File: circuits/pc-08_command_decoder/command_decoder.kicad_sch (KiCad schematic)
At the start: 17 parts, among them U1 74HC138, U2 74HC138, U3 74HC138, U4 74HC138, U5 4011, U6 4011, U7 74HC138, U8 4011

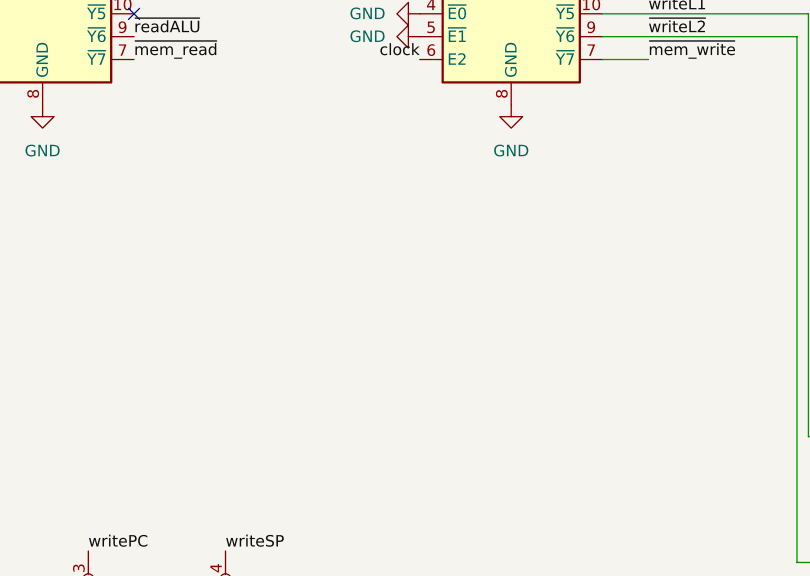
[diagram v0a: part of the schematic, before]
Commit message: add pull-up resistor network to command decoder
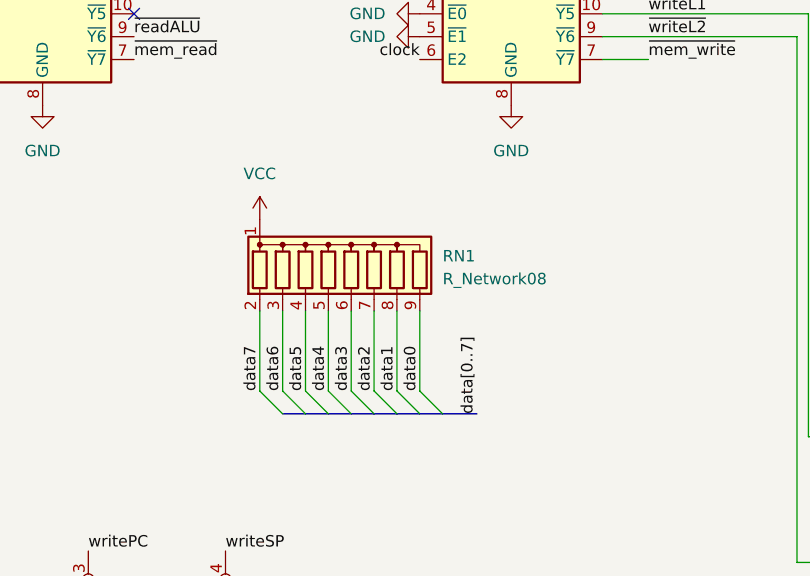
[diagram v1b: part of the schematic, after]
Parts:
- added RN1: R_Network08, Resistor_THT:R_Array_SIP9, symbol Device:R_Network08
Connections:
- net VCC: now also RN1.1 (common)
- net data0: now also RN1.9 (R8)
- net data1: now also RN1.8 (R7)
- net data2: now also RN1.7 (R6)
- net data3: now also RN1.6 (R5)
- net data4: now also RN1.5 (R4)
- net data5: now also RN1.4 (R3)
- net data6: now also RN1.3 (R2)
- net data7: now also RN1.2 (R1)

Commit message: pc08: finishing touches and interconnects
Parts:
- added D1: LED, LED_SMD:LED_0603_1608Metric, symbol Device:LED
- added J1: Screw_Terminal_01x02, TerminalBlock_TE-Connectivity:TerminalBlock_TE_282834-2_1x02_P2.54mm_Horizontal, symbol Connector:Screw_Terminal_01x02
- added J2: Conn_01x06, Connector_PinHeader_2.54mm:PinHeader_1x06_P2.54mm_Vertical, symbol Connector_Generic:Conn_01x06
- added J3: Conn_01x03, Connector_PinHeader_2.54mm:PinHeader_1x03_P2.54mm_Vertical, symbol Connector_Generic:Conn_01x03
- added J4: Conn_01x08, Connector_PinHeader_2.54mm:PinHeader_1x08_P2.54mm_Vertical, symbol Connector_Generic:Conn_01x08
- added J5: Conn_01x05, Connector_PinHeader_2.54mm:PinHeader_1x05_P2.54mm_Vertical, symbol Connector_Generic:Conn_01x05
- added J6: Conn_01x07, Connector_PinHeader_2.54mm:PinHeader_1x07_P2.54mm_Vertical, symbol Connector_Generic:Conn_01x07
- added R1: 1K, Resistor_SMD:R_0603_1608Metric, symbol Device:R
- added RN2, RN3: R_Network08, Resistor_THT:R_Array_SIP9, symbol Device:R_Network08
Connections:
- net GND: now also J1.1 (Pin_1), J6.7 (Pin_7), R1.2, RN2.1 (common), RN3.1 (common)
- net VCC: now also D1.2 (A), J1.2 (Pin_2), J6.1 (Pin_1)
- net action0: now also RN2.9 (R8)
- net action1: now also RN2.8 (R7)
- net action2: now also RN2.7 (R6)
- net action3: now also RN2.6 (R5)
- net action4: now also RN2.5 (R4)
- net asrc0: now also RN2.4 (R3)
- net asrc1: now also RN2.3 (R2)
- net asrc2: now also RN2.2 (R1)
- net carryFlag: now also J5.1 (Pin_1)
- net clock: now also J6.5 (Pin_5), RN3.2 (R1)
- net data0: now also J4.1 (Pin_1)
- net data1: now also J4.2 (Pin_2)
- net data2: now also J4.3 (Pin_3)
- net data3: now also J4.4 (Pin_4)
- net data4: now also J4.5 (Pin_5)
- net data5: now also J4.6 (Pin_6)
- net data6: now also J4.7 (Pin_7)
- net data7: now also J4.8 (Pin_8)
- net dsrc0: now also J5.2 (Pin_2), RN3.9 (R8)
- net dsrc1: now also J5.3 (Pin_3), RN3.8 (R7)
- net dsrc2: now also J5.4 (Pin_4), RN3.7 (R6)
- net dsrc3: now also J5.5 (Pin_5), RN3.6 (R5)
- net dtgt0: now also J6.2 (Pin_2), RN3.5 (R4)
- net dtgt1: now also J6.3 (Pin_3), RN3.4 (R3)
- net dtgt2: now also J6.4 (Pin_4), RN3.3 (R2)
- net ~{reset}: now also J6.6 (Pin_6)
- net at U1.7 (~{Y7}): now also J3.1 (Pin_1)
- net at U7.10 (~{Y5}): now also J2.4 (Pin_4)
- net at U7.11 (~{Y4}): now also J2.3 (Pin_3)
- net at U7.12 (~{Y3}): now also J2.2 (Pin_2)
- net at U7.13 (~{Y2}): now also J2.1 (Pin_1)
- net at U7.7 (~{Y7}): now also J2.6 (Pin_6)
- net at U7.9 (~{Y6}): now also J2.5 (Pin_5)
- net at U2.10 (~{Y5}): now also J3.2 (Pin_2)
- net at U2.11 (~{Y4}): now also J3.3 (Pin_3)
- new net: D1.1 (K), R1.1
- no-connect marks 16 -> 7
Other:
- moved on the sheet: RN1

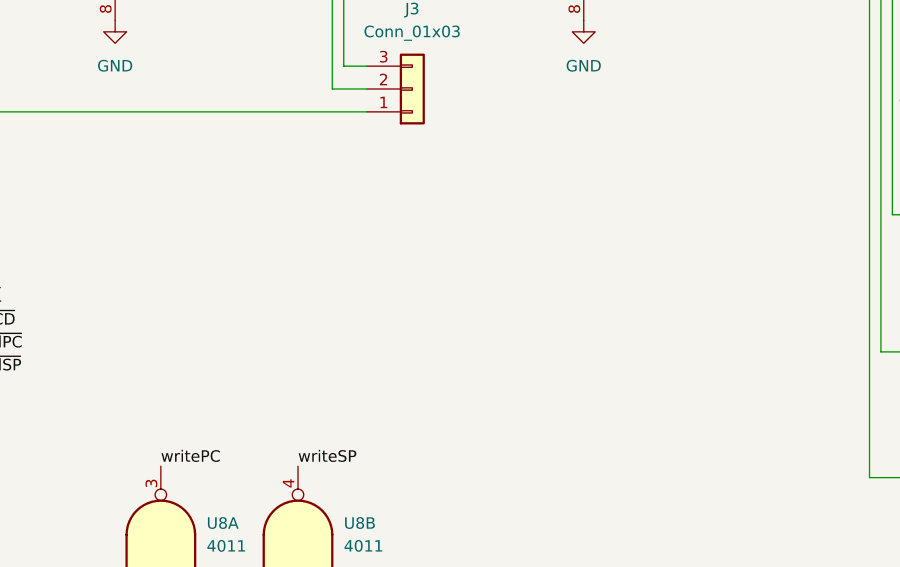
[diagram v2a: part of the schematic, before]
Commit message: add filter and decoupling capacitors to all boards
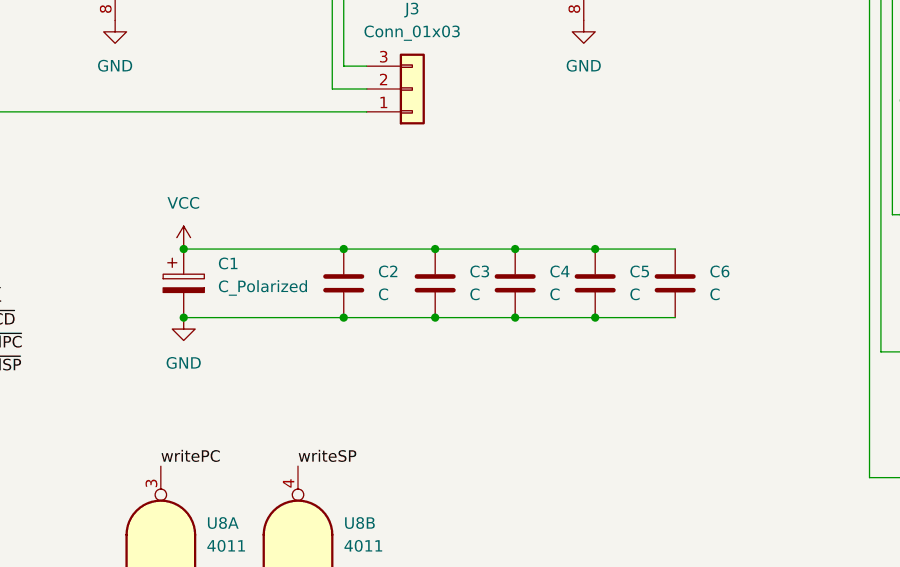
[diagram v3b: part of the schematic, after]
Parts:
- added C1: C_Polarized, Capacitor_SMD:CP_Elec_5x5.3, symbol Device:C_Polarized
- added C2, C3, C4, C5, C6: C, Capacitor_SMD:C_0603_1608Metric, symbol Device:C
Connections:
- net GND: now also C1.2, C2.2, C3.2, C4.2, C5.2, C6.2
- net VCC: now also C1.1, C2.1, C3.1, C4.1, C5.1, C6.1
